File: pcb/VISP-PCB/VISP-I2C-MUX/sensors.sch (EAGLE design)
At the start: 41 parts, among them IC1 BMP388, IC2 BMP388, IC3 BMP388, IC4 BMP388, U1 MIC5225-3.3, U2 TCA9546APWR, U3 24C01ASM, U5 BMP280, U6 BMP280, U7 BMP280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

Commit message: Update I2C MUX board for VISP. Now, it can support a sensor on every pad (for direct comparison analysis) Lowered I2C pullup values.   Each sensor is on it's own I2C bus behind the MUX Wire pads have been brought out to the sides of the OLED pins for somewhat easier wiring
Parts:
- removed C10, C11, C12, C8: 100nF, Capacitor:CAPACITOR-1206
- removed GND, SCL, SDA, VCC: (no value), wirepad:SMD2
- removed SV1: (no value), con-lstb:MA04-1
- added C2: 100nF, Capacitor:CAPACITOR-0402
- added GOLD_ORB_SM1: OSHWLOGOLOGO8MM, oshw:OSHWLOGOLOGO8MM
- added JP4: (no value), pinhead-2:PINHD-1X08_2.54
- added R10, R11, R8, R9: 2k7, Resistor:RESISTOR-0402
- added R12, R13: 4k7, Resistor:RESISTOR-0402
- C1, C3: device microbuilder:CAP_CERAMIC0603_NO -> microbuilder:CAP_CERAMIC_0805
- C9: device Capacitor:CAPACITOR-0603 -> Capacitor:CAPACITOR-0402
- R1, R2, R22, R23: value 10K Ohms -> 2k7; device Resistor:RESISTOR-0603 -> Resistor:RESISTOR-0402
- R3, R4, R5, R6, R7: device Resistor:RESISTOR-0603 -> Resistor:RESISTOR-0402
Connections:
- new net SCK3_3V: IC3.SCK, IC4.SCK, R10.1, U2.SC2
- new net SCK4_3V: IC1.SCK, IC2.SCK, R11.1, U2.SC3
- new net SDI3_3V: IC3.SDI, IC4.SDI, R8.1, U2.SD2
- new net SDI4_3V: IC1.SDI, IC2.SDI, R9.1, U2.SD3
- net 3.3V: now also R10.2, R11.2, R8.2, R9.2; no longer C10.C1, C11.C1, C12.C1, C8.C1, C9.C1, U3.A2, U3.VCC
- net 5.0V: now also C2.C1, C9.C1, JP4.5, JP4.8, R12.2, R13.2, U3.VCC; no longer SV1.3, VCC.P
- net A0: now also U3.A0
- net A1: now also U3.A1
- net A2: now also U3.A2
- net GND: now also C2.C2, JP4.6, JP4.7; no longer C10.C2, C11.C2, C12.C2, C8.C2, GND.P, SV1.4, U3.A0, U3.A1
- net SCK1_3V: no longer IC3.SCK, IC4.SCK, U3.SCL
- net SCK2_3V: no longer IC1.SCK, IC2.SCK
- net SCL_5V: now also JP4.1, JP4.4, R13.1, U3.SCL; no longer SCL.P, SV1.2
- net SDA_5V: now also JP4.2, JP4.3, R12.1, U3.SDA; no longer SDA.P, SV1.1
- net SDI1_3V: no longer IC3.SDI, IC4.SDI, U3.SDA
- net SDI2_3V: no longer IC1.SDI, IC2.SDI
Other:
- note added: "Copyright 2020 Steven Carr and Daren Schwenke No warranty expressed or implied I2C MUX Sensor Package for VISP"
- note added: "V0.2"
- note removed: "Alternate 1206 Bypass Caps (U5->U8)"
- note removed: "Copyright 2020 Steven Carr and Daren Schwenke No warranty expressed or implied I2C MUX Pitot Tube Sensor Package for VISP"
- note removed: "I2C Addr 0x54"
- note removed: "V0.1"
- moved on the sheet: C4, C5, C6, C7

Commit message: Update VISP-I2C-MUX for manufacturing by OSH-Park All 8 sensor pads can be populated simultaneously without I2C bus conflicts. Updated board text to reflect new capabilities Increased width slightly to satisfy OSH-parks 2-Layer rules.
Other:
- note added: "I2C BUS3"
- note added: "I2C BUS4"
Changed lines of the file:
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@@
 <?xml version="1.0" encoding="utf-8"?>
 <!DOCTYPE eagle SYSTEM "eagle.dtd">
-<eagle version="7.7.0">
+<eagle version="7.6.0">
 <drawing>
 <settings>
@@
 <text x="182.88" y="2.54" size="1.778" layer="91">I2C Addr 0x77</text>
 <text x="182.88" y="5.08" size="1.778" layer="91">PITOT TUBES</text>
-<text x="17.78" y="7.62" size="1.778" layer="91">I2C BUS1</text>
+<text x="17.78" y="7.62" size="1.778" layer="91">I2C BUS3</text>
 <text x="17.78" y="38.1" size="1.778" layer="91">I2C BUS1</text>
 <text x="71.12" y="38.1" size="1.778" layer="91">I2C BUS1</text>
-<text x="71.12" y="7.62" size="1.778" layer="91">I2C BUS1</text>
+<text x="71.12" y="7.62" size="1.778" layer="91">I2C BUS3</text>
 <text x="129.54" y="40.64" size="1.778" layer="91">I2C BUS2</text>
-<text x="129.54" y="7.62" size="1.778" layer="91">I2C BUS2</text>
-<text x="182.88" y="7.62" size="1.778" layer="91">I2C BUS2</text>
+<text x="129.54" y="7.62" size="1.778" layer="91">I2C BUS4</text>
+<text x="182.88" y="7.62" size="1.778" layer="91">I2C BUS4</text>
 <text x="182.88" y="40.64" size="1.778" layer="91">I2C BUS2</text>
 </plain>

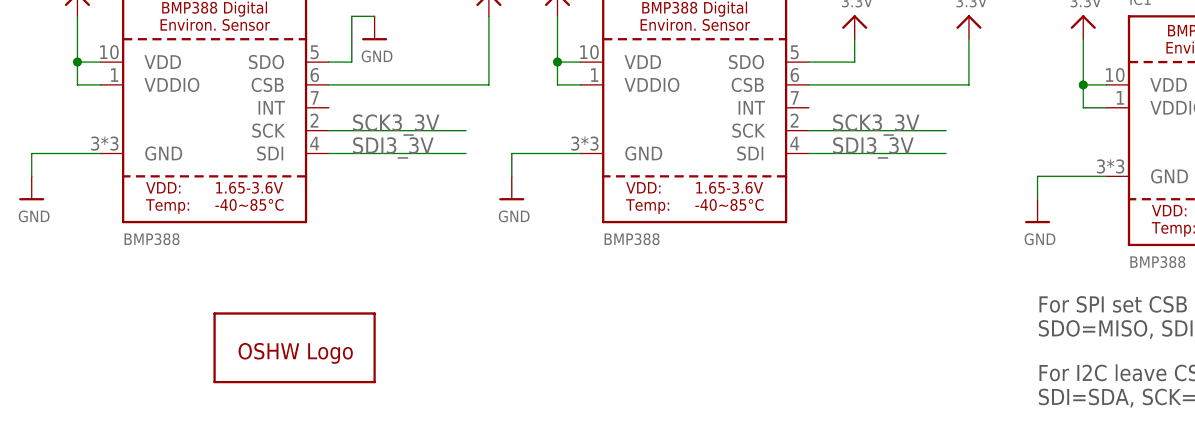
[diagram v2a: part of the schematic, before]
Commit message: Update notes in schematics for VISP PCB's
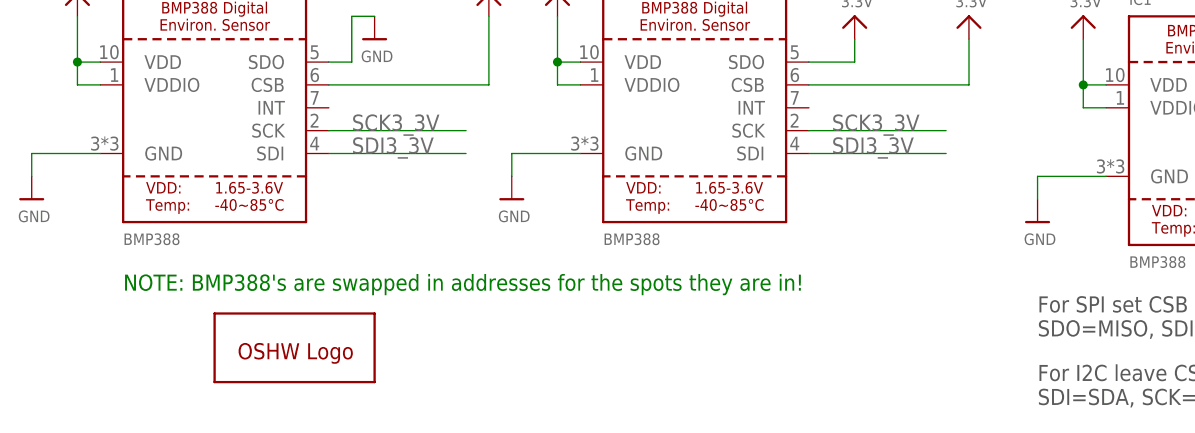
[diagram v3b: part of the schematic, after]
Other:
- note added: "NOTE: BMP388's are swapped in addresses for the spots they are in!"
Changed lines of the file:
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@@
 <text x="182.88" y="7.62" size="1.778" layer="91">I2C BUS4</text>
 <text x="182.88" y="40.64" size="1.778" layer="91">I2C BUS2</text>
+<text x="12.7" y="-30.48" size="1.778" layer="91">NOTE: BMP388's are swapped in addresses for the spots they are in!</text>
 </plain>
 <instances>

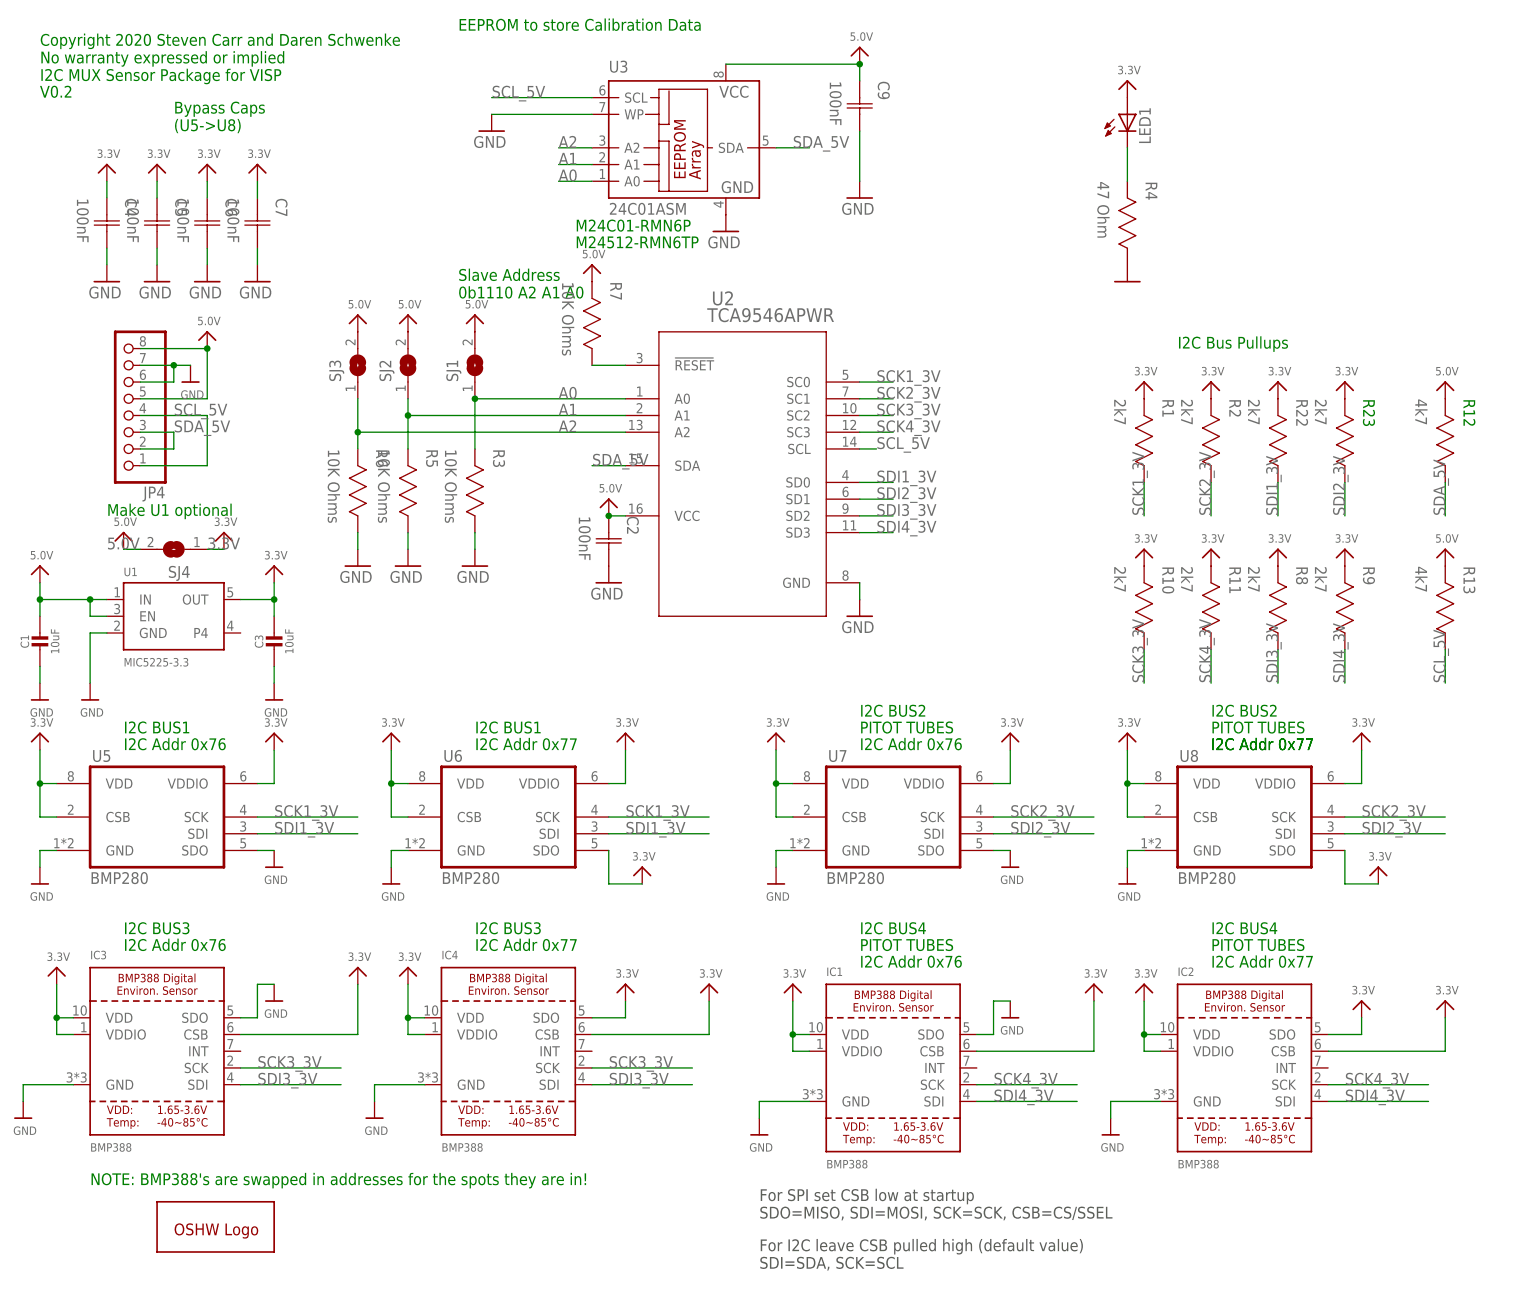
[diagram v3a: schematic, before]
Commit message: Add BME680 footprints.   Rearrange sensors on the buses to match each other. Bus1 is 2 sensors in same hole, all BMP388's are I2C:0x76 and BME680's are I2C:0x77
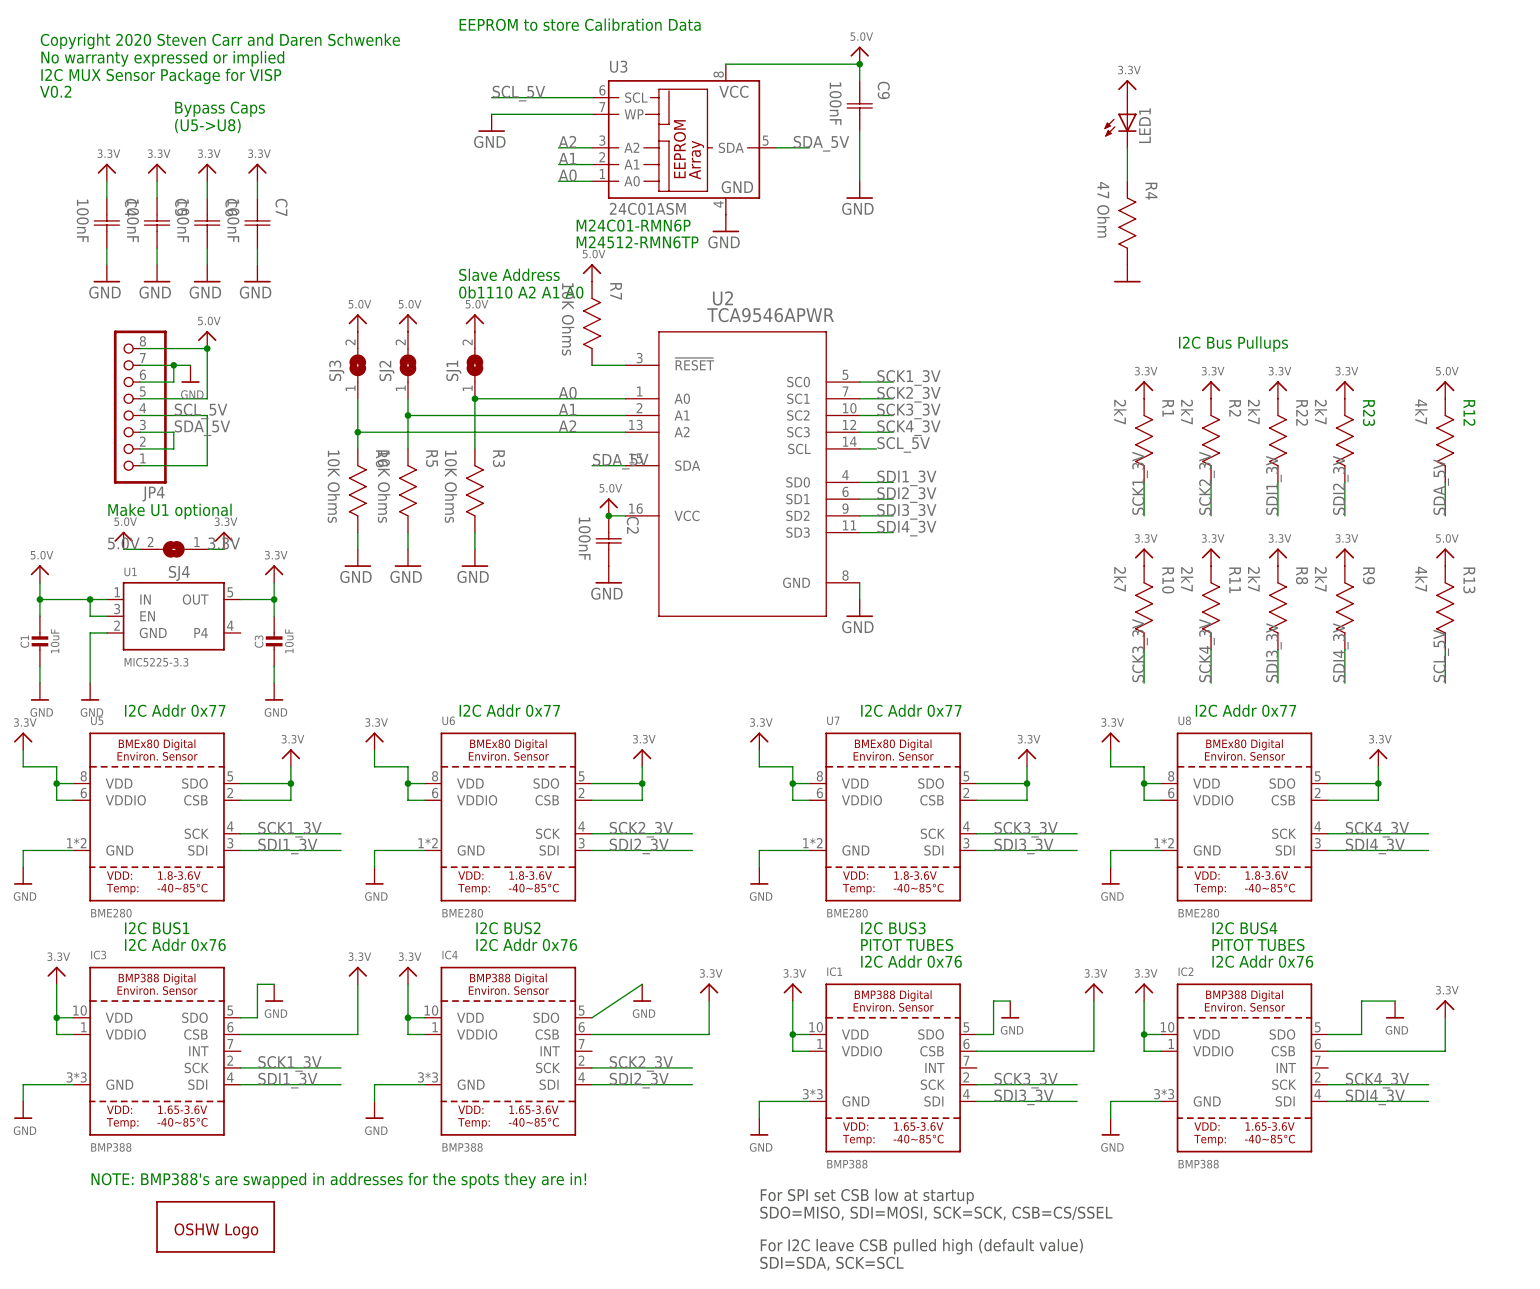
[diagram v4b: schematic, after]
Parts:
- U5, U6, U7, U8: value BMP280 -> BME280; device bosch-bmp280:BMP280 -> microbuilder:BME280; MPN BMP280 -> (none)
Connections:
- net 3.3V: now also U5.SDO, U7.SDO; no longer IC2.SDO, IC4.SDO
- net GND: now also IC2.SDO, IC4.SDO; no longer U5.SDO, U7.SDO
- net SCK1_3V: now also IC3.SCK; no longer U6.SCK
- net SCK2_3V: now also IC4.SCK, U6.SCK; no longer U7.SCK, U8.SCK
- net SCK3_3V: now also IC1.SCK, U7.SCK; no longer IC3.SCK, IC4.SCK
- net SCK4_3V: now also U8.SCK; no longer IC1.SCK
- net SDI1_3V: now also IC3.SDI; no longer U6.SDI
- net SDI2_3V: now also IC4.SDI, U6.SDI; no longer U7.SDI, U8.SDI
- net SDI3_3V: now also IC1.SDI, U7.SDI; no longer IC3.SDI, IC4.SDI
- net SDI4_3V: now also U8.SDI; no longer IC1.SDI
